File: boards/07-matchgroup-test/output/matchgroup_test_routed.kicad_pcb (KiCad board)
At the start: 4 copper layers, 110 x 95 mm, 8 parts, among them J1 FFC6_MIPI, J2 HDMI19, J3 ADDR_HDR, U1 QFN48_DDR_CTRL, U2 QFN48_DRAM, U3 QFN24_MIPI, U4 BGA49_HDMI, U5 QFP48_SRAM

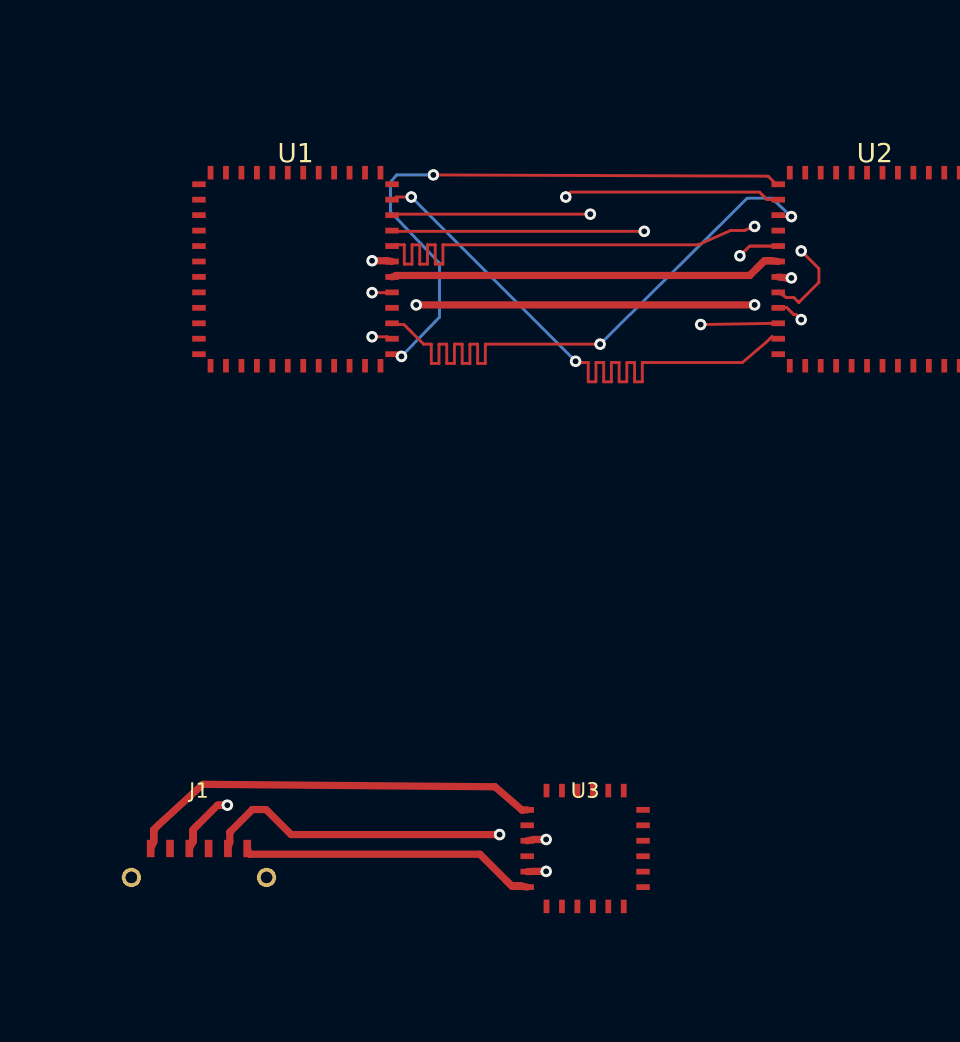
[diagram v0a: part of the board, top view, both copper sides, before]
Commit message: fix(router): convergence requires all nets routed, not just overflow==0
The negotiated loop declared "Convergence achieved" at overflow==0 with
nets still stranded, abandoning most of the wall budget (board 07: exit
at ~820s of a 1500s budget with 3 nets unrouted).  The count predicate
``len(net_routes) == total_nets`` was wrong on two counts:

1. ``rip_up_nets`` leaves ``net_routes[n] == []`` behind, so a net that
   was ripped up and then hard-failed its re-route (instant empty A*
   frontier => ZERO overflow, e.g. DQ3 in 0.04s) still counted as routed.
2. A multi-pad net whose main A* failed can sit in ``net_routes`` with
   partial fragments (subset of MST edges) connecting only some pads.

Fixes:
- New ``_stranded_nets()`` predicate (union-find pad connectivity over
  routable nets) gates all four "Convergence achieved" break sites, the
  iteration-0 "No conflicts - routing complete!" early return, and the
  final progress-callback status (now ``stranded`` instead of
  ``converged`` when overflow==0 with stranded nets).
- Empty-list entries now count as failed throughout the recovery
  machinery: failed_nets_to_recover (#858), zero-overflow elevated-cost
  recovery (#2396), stagnation-recovery re-add (#2515), targeted
  fallback still_failed (#2265), BLOCKED_BY_COMPONENT recomputes, and
  the ``should_terminate_early`` unrouted_count guard (#2297).

Board 07 (seed 42, 600s recipe): 28/31 -> 29/31, budget now fully
consumed (598.9s vs ~453s premature exit); matchgroup CI gate green
(21 raw DRC <= 25 allowlist; routed-drc gate 16 blocking <= 25).
Refreshed routed artifact included.  Boards 02 (8/8), 03 (12/13),
04 (9/9), softstart reach floor (>=6/10) all hold.

Refs #3438. Refs #3414.

Closes #3448

Co-Authored-By: Claude Opus 4.7 <noreply@anthropic.com>
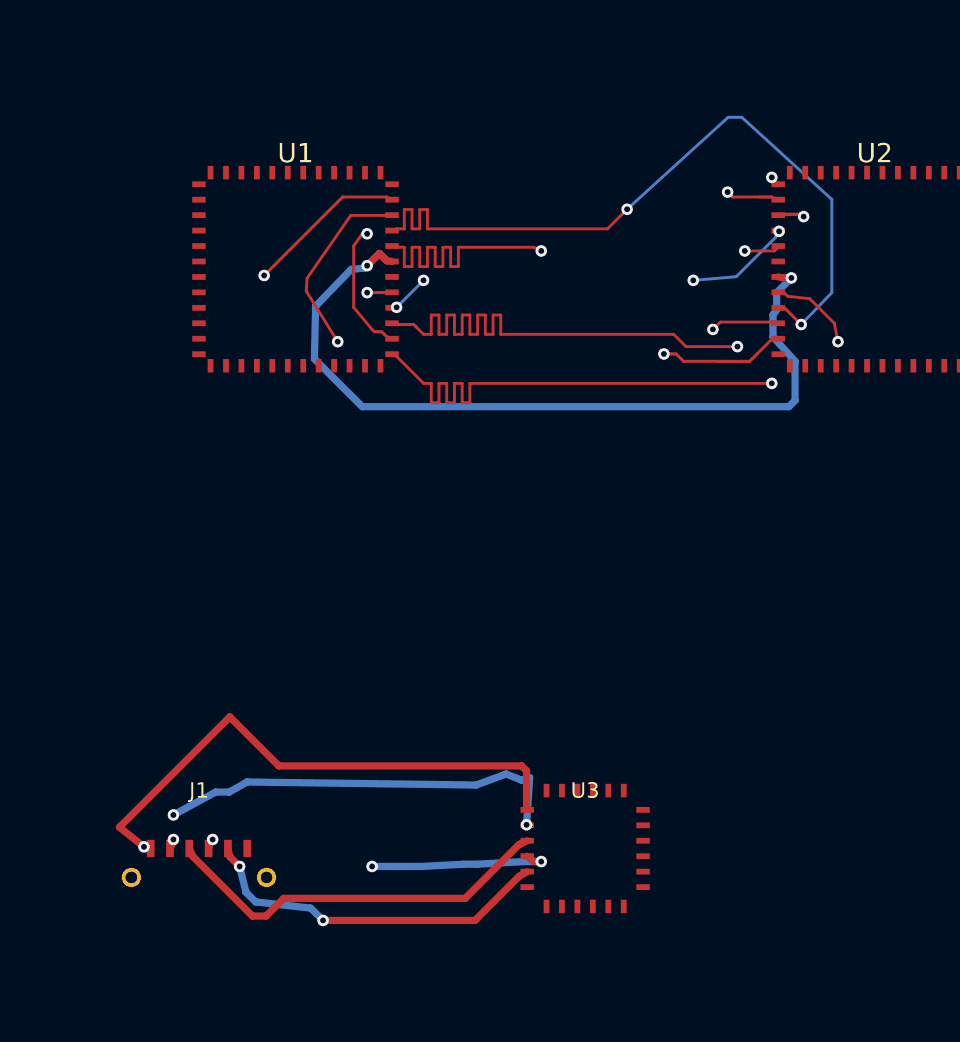
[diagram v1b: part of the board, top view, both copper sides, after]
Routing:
- net DQ3: track 0.00 -> 39.7 mm, vias 0 -> 4
- net MIPI_CLK_N: track 0.00 -> 23.3 mm, vias 0 -> 3
- net DQS_P: track 20.3 -> 0.00 mm
- net MIPI_DAT0_N: track 0.00 -> 19.0 mm, vias 0 -> 3
- net DQS_N: track 25.0 -> 41.9 mm, vias 4 -> 2
- net MIPI_DAT1_N: track 15.4 -> 0.00 mm
- net DQ6: track 32.4 -> 40.9 mm
- net DQ0: track 31.8 -> 39.9 mm
- net DQ4: track 32.6 -> 40.6 mm
- net DQ1: track 33.3 -> 40.8 mm
- net DQ2: track 33.3 -> 40.6 mm
- net DM0: track 32.6 -> 39.7 mm
- net DQ7: track 32.1 -> 39.1 mm
- net MIPI_CLK_P: track 21.7 -> 28.6 mm, vias 0 -> 1
- net DQ5: track 32.8 -> 39.4 mm
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
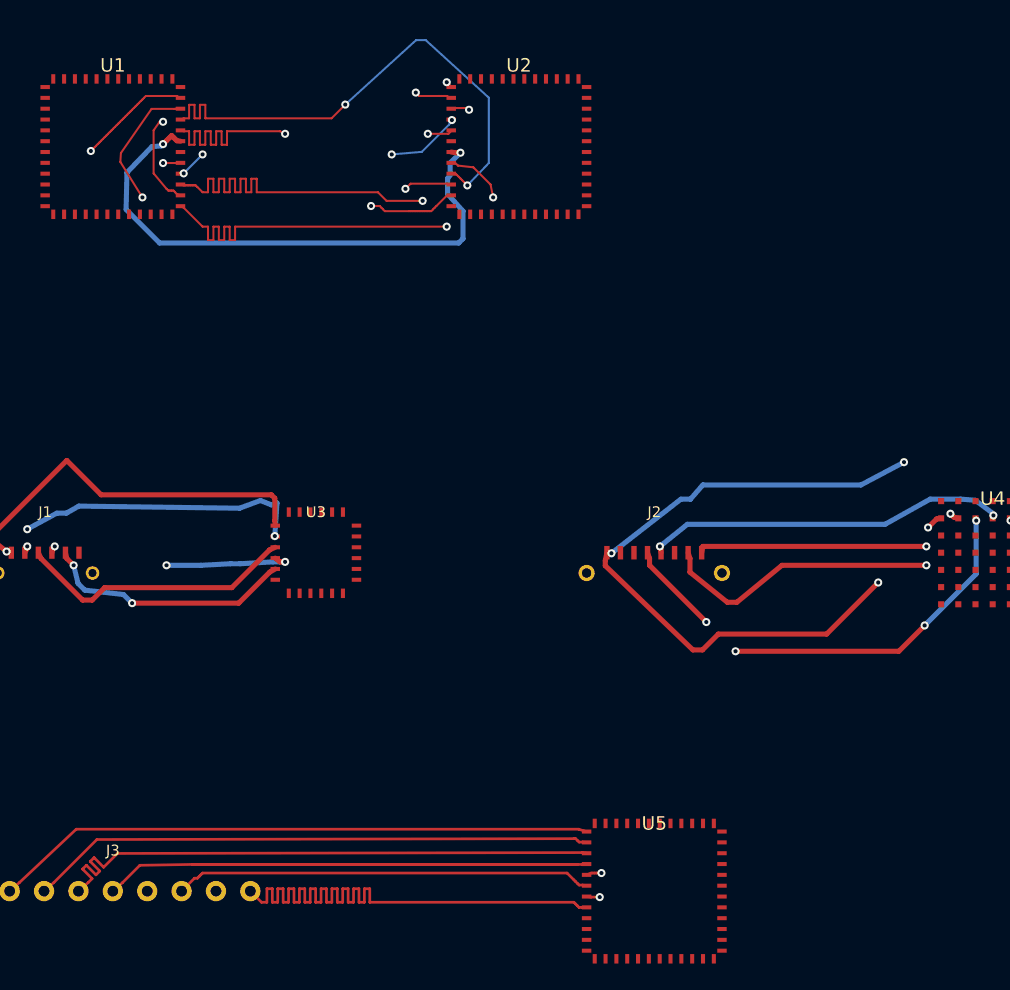
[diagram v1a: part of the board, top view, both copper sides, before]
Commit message: fix(router): match-group reference semantics + distributed meanders + reason-bucket observability (closes #3440)
Three coordinated fixes for the board 07 ADDR_BUS 15.395mm skew:

1. Reference semantics: when the declared pace-car reference routes
   shorter than another member by more than tolerance, the lengthen-only
   tuner auto-promotes longest-in-group as the effective reference
   (structured warning logged); strict pace-car behavior preserved when
   the declaration is satisfiable.

2. Meander capacity (distributed meanders): descending amplitude
   back-off ladder (1.0/0.5/0.25/0.125 x base) with exact-fit amplitude
   (no more 2*amplitude overshoot quanta), collinear-merge normalization
   so A* staircase routes expose multi-mm host segments, a fallback
   one-loop host floor for heavily jogged routes, and a routes_by_net
   staleness fix so later members' DRC self-checks see earlier members'
   committed meanders (plus the matching commit-back identity-guard fix
   in core.py so meanders actually reach the saved PCB).

3. Observability: both summary printers count EVERY TuneResult.reason
   via a shared registry-driven formatter (reference/longer-than-ref/
   unrouted/no-segment buckets can no longer vanish); rollbacks log the
   violated rule + neighbor + capacity shortfall; loud stderr warnings
   when --length-match-groups or the skew DRC rules are inactive for
   lack of a net-class map; intra-pair clearance clamped to the
   intra-group floor (impedance-resolver ~8mm coupling gaps falsely
   rejected every pair meander).

Board 07 (production recipe, seed 42): ADDR_BUS skew 15.395mm -> 0.004mm
(tol 0.5mm); DDR_DATA_BYTE_0 within its 0.1mm tolerance; both
match_group_length_skew DRC errors gone (21 -> 19 total errors,
allowlist 21). Committed routed artifact refreshed; parity test
re-baselined (blocking 16 -> 14).

Co-Authored-By: Claude Opus 4.7 <noreply@anthropic.com>
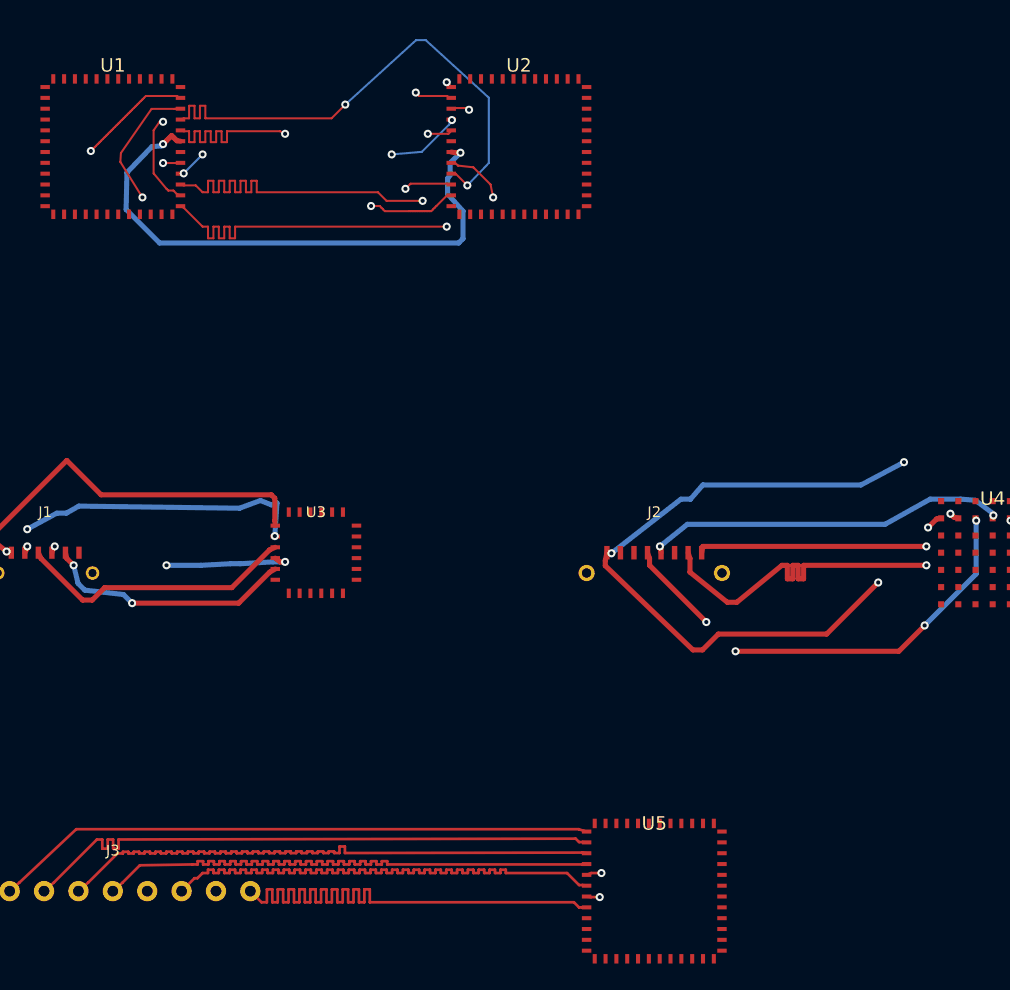
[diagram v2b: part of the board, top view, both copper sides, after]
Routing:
- net A5: track 30.8 -> 44.4 mm
- net A4: track 35.2 -> 44.4 mm
- net A3: track 35.8 -> 44.4 mm
- net TMDS_D2_P: track 28.6 -> 32.6 mm
- net A1: track 41.7 -> 44.4 mm
- net DQ6: track 40.9 -> 39.1 mm
- net A6: track 46.2 -> 44.4 mm
- net A2: track 42.7 -> 44.4 mm
- net DQ1: track 40.8 -> 39.1 mm
- net DQ4: track 40.6 -> 39.1 mm
- net DQ2: track 40.6 -> 39.1 mm
- net A7: track 45.3 -> 44.4 mm
- net DQ0: track 39.9 -> 39.1 mm
- net DQ3: track 39.7 -> 39.1 mm
- net DM0: track 39.7 -> 39.1 mm

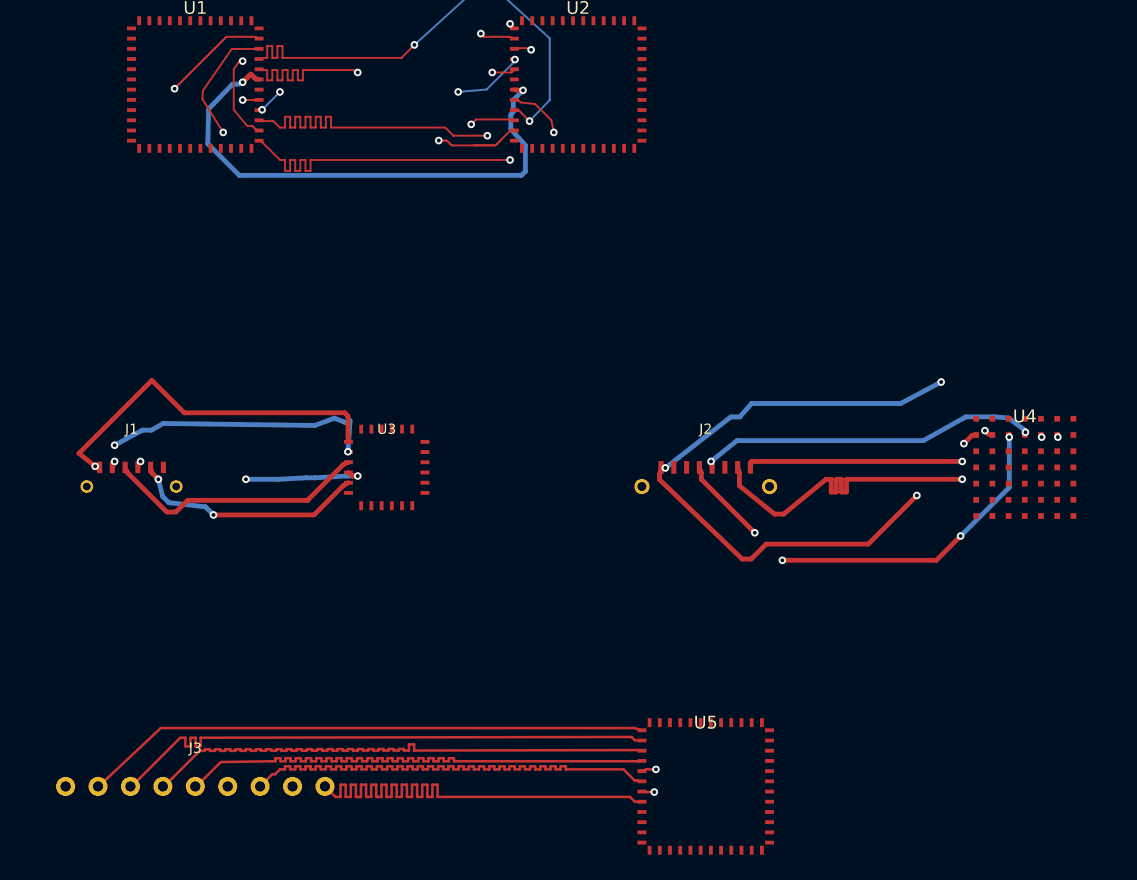
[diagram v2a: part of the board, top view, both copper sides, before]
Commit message: fix(router): 45° quantization in post-route mutation passes (closes #3532)
204/4519 segments on softstart's committed routed artifact sat 0.8-22.5°
off the 0/45/90/135 set; every fleet board carried the same class
(board 07: 297/909). Attribution: 127 pad-tail emissions (the C++
reconstruct_path / Python _convert_path_to_route connect the last grid
cell to the exact off-grid pad centre with one skewed segment), 41
step-10c/d repair chain drags (regex endpoint dragging in
generate_design.py), 36 optimizer mutations (pull-tight neighbour
re-aiming, chamfer terminal restoration).

Fixes at source, all sharing the new router/quantize.py helpers
(is_45_aligned / snap_direction_8 / dogleg_points / quantize_pcb_file):

* cpp_backend._convert_result_to_route splits skewed C++ tails into
  exact float64 doglegs (C++ float32 ulp is too coarse for exact legs)
* Python Router._convert_path_to_route emits dogleg pad tails; the
  extend-to-pad branch requires the extended segment to stay aligned
* convert_corners_45 terminal restoration emits doglegs, not skews
* pull_tight_pass declines windows whose neighbours are not parallel
  to the translation direction (the classic H-V-H jog still compresses)
* drc_nudge segment/via chain snaps decline drags that would skew an
  abutting segment off the 45° set
* softstart recipe: step-10c via slides snap to the 8-direction set;
  new step-10e runs quantize_pcb_file before the DRC gate

Committed artifacts repaired in place with the exact-decimal
quantize_pcb_file (dogleg endpoints preserved bit-for-bit, second-leg
uuids deterministic uuid5). Fleet census ratchet in
tests/test_fleet_45_census.py: softstart + boards 01-05 at 0 off-angle;
documented residuals (issue #3535) are 2 corridor chords where both
dogleg variants collide (06/07) and board 07's 55 DDR_DATA_BYTE_0
length-tuning meanders (doglegging breaks the exactly-tuned
match_group_length_skew).

DRC: softstart 0 violations at jlcpcb-tier1 (strict gate; manufacturers
override added 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
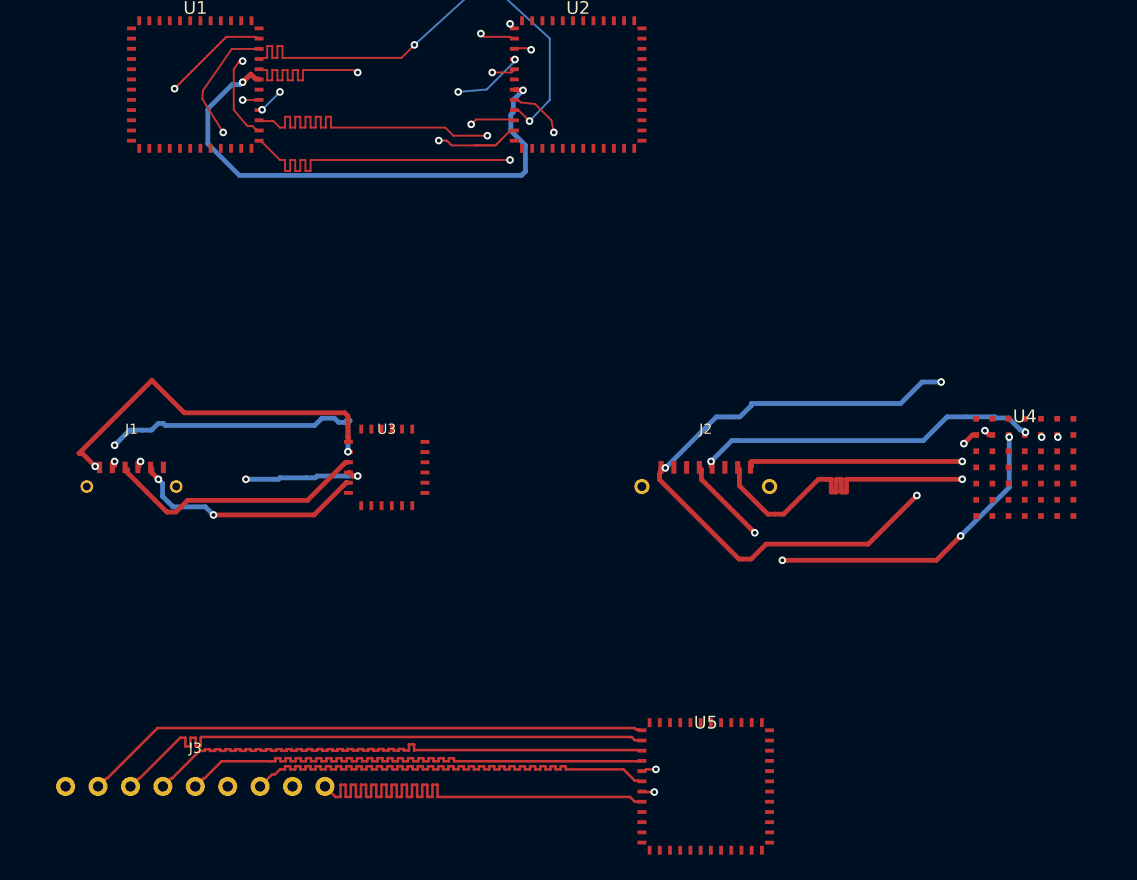
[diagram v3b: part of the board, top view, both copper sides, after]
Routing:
- net TMDS_D0_N: track 29.7 -> 30.4 mm
- net MIPI_CLK_N: track 23.3 -> 24.0 mm
- net TMDS_D1_N: track 26.8 -> 27.4 mm
